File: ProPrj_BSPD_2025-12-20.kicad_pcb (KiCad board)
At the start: 2 copper layers, 49 parts

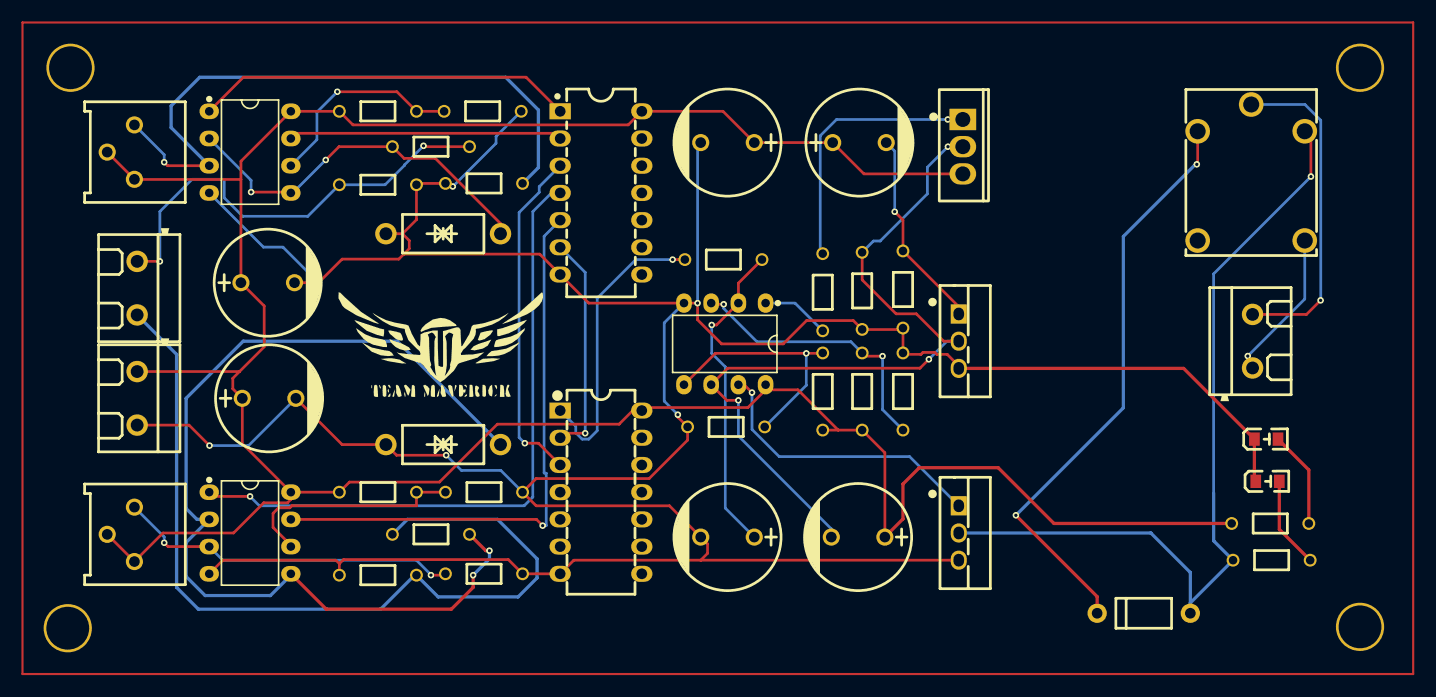
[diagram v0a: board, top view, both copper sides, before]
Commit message: pcb border layer change
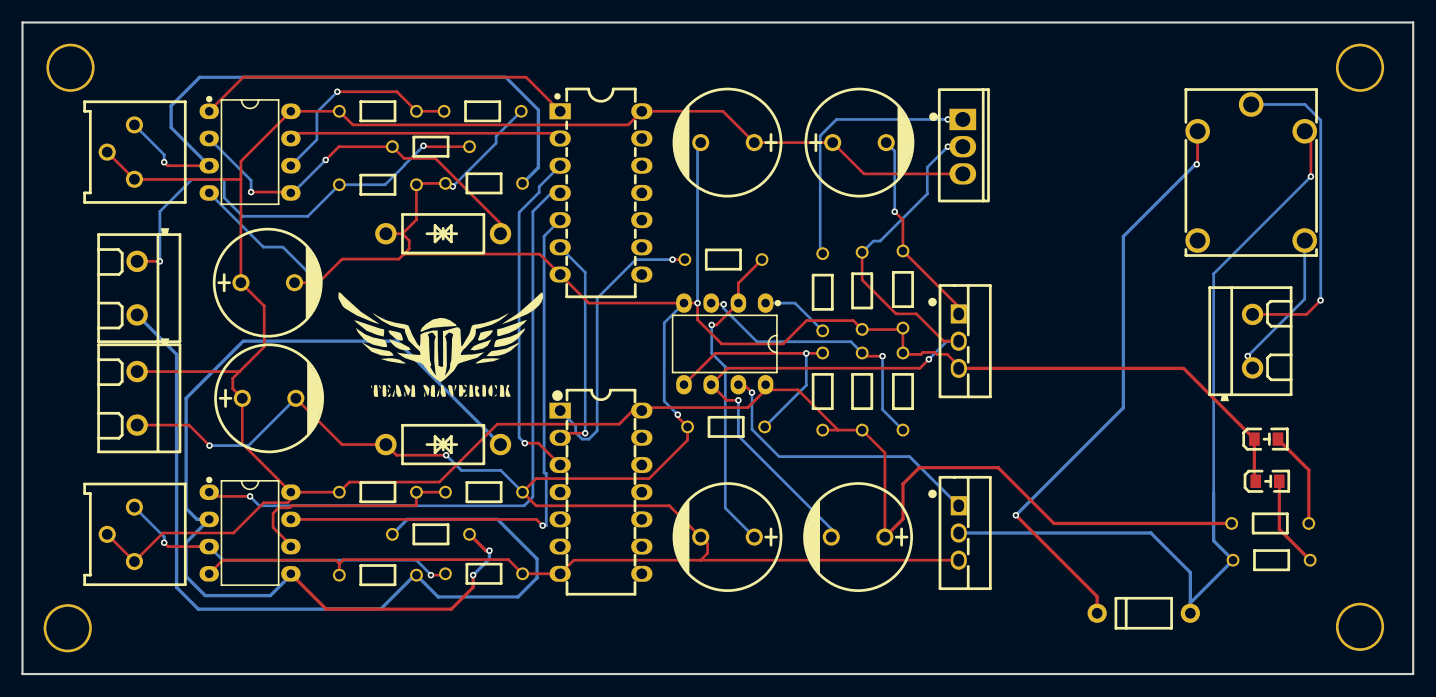
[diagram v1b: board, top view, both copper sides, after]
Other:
- board outline added: 129.8 x 60.8 mm
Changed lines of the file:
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@@
 		)
-	)
-	(gr_rect
-		(start 77.67 33.07)
-		(end 207.51 93.9)
-		(stroke
-			(width 0.2)
-			(type default)
-		)
-		(fill no)
-		(layer "F.Cu")
 	)
 	(gr_poly
@@
 		(layer "F.SilkS")
 	)
+	(gr_rect
+		(start 77.67 33.07)
+		(end 207.51 93.9)
+		(stroke
+			(width 0.2)
+			(type solid)
+		)
+		(fill no)
+		(layer "Edge.Cuts")
+	)
 	(segment
